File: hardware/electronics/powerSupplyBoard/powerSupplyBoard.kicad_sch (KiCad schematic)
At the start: 8 parts, among them J1 Barrel_Jack_Switch, J2 VAL, J3 VAL, J4 VAL

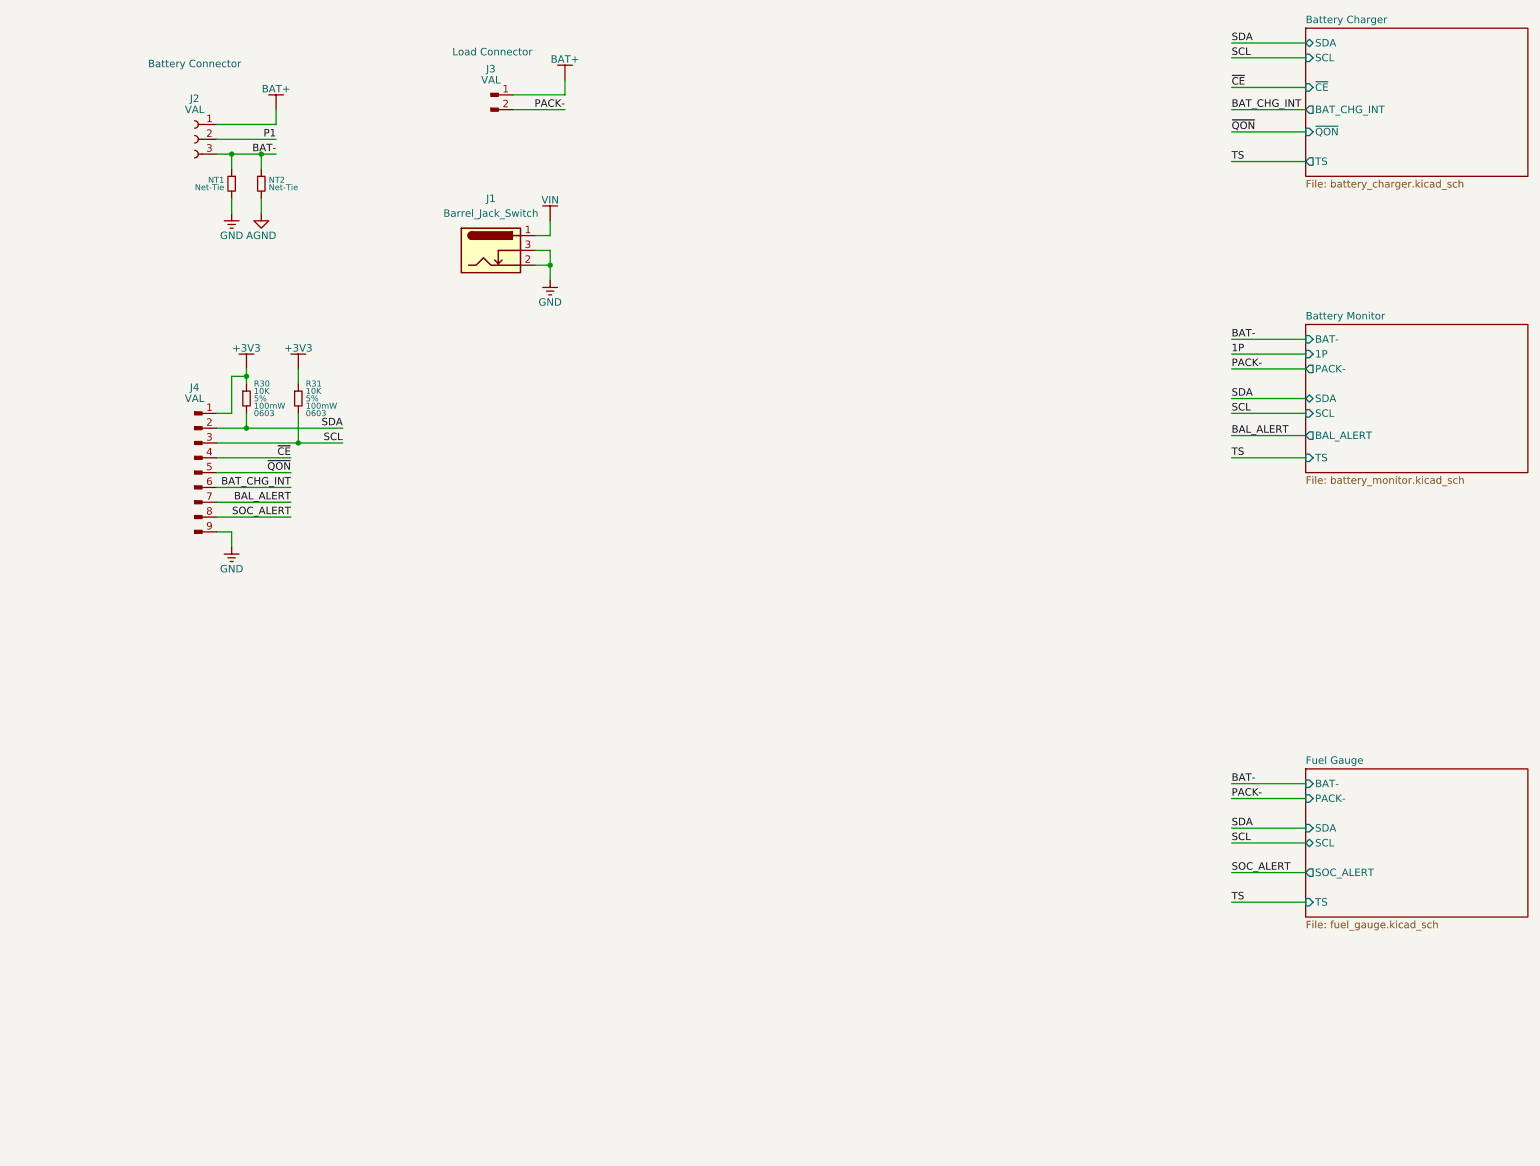
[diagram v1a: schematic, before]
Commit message: added basic sch for stm32l4
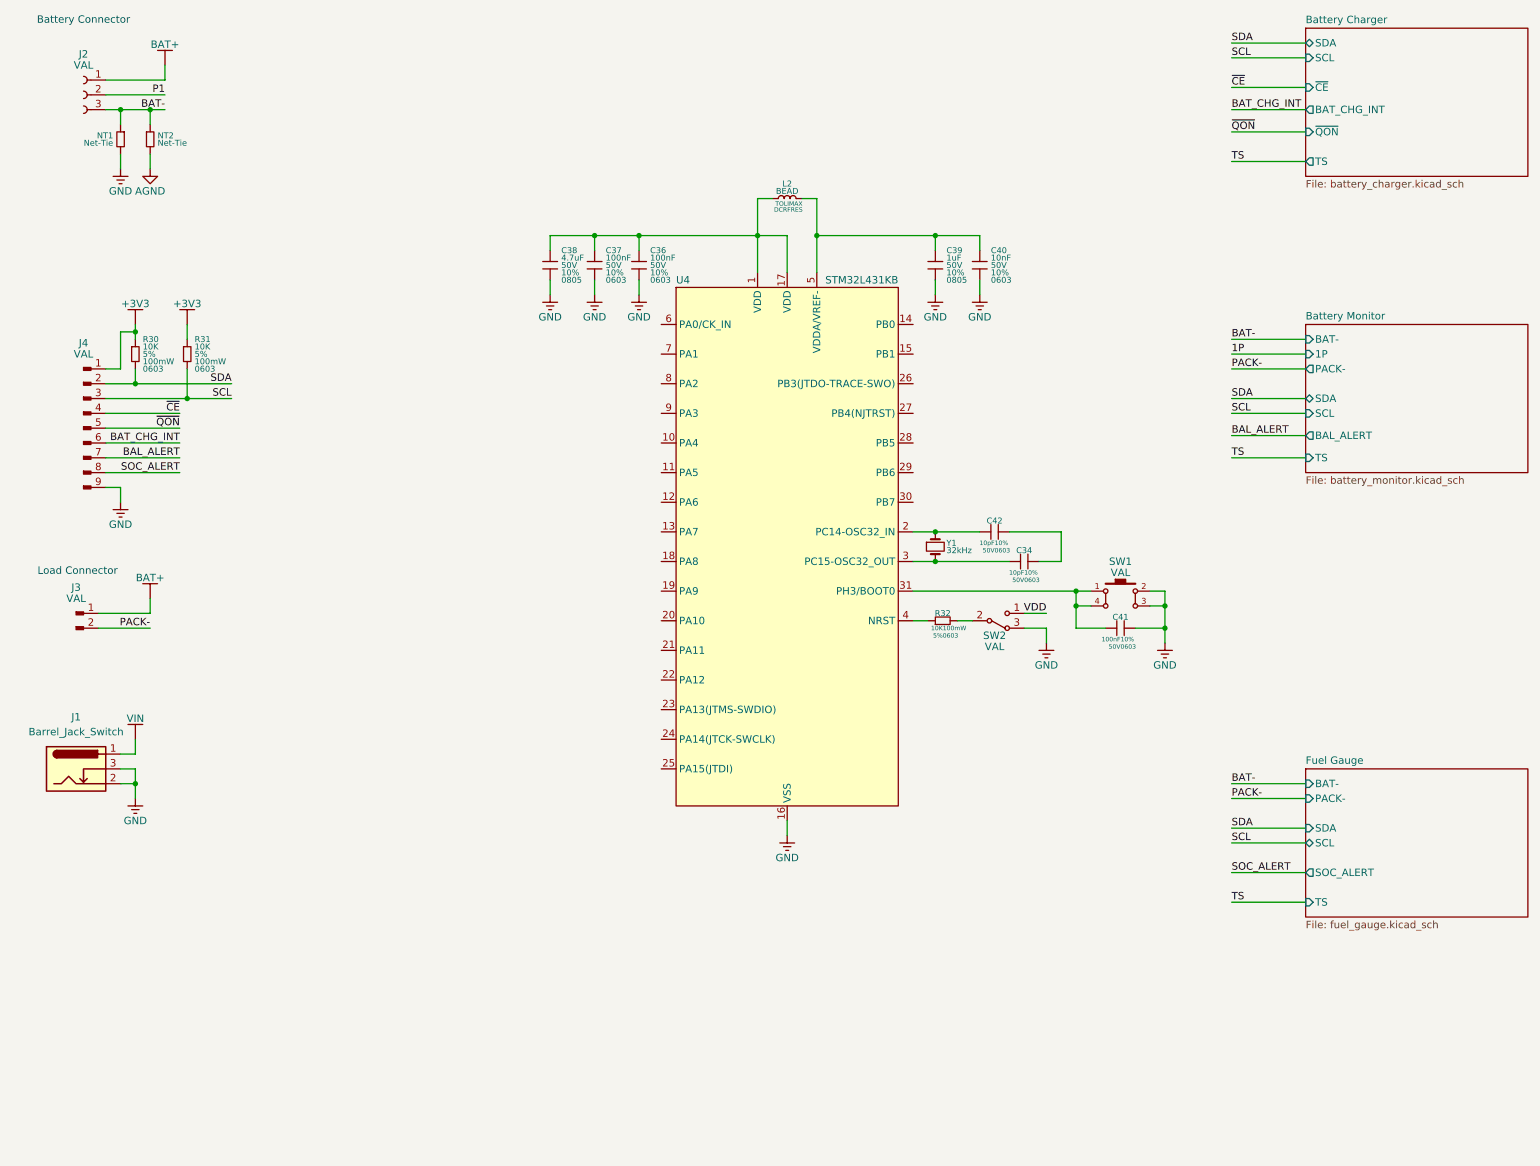
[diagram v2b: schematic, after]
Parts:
- added C34, C42: 10pF, DS-Capacitors-SMD:MLCC0603, symbol DS-Passives:C_horizontal
- added C36, C37: 100nF, DS-Capacitors-SMD:MLCC0603, symbol DS-Passives:C
- added C38: 4.7uF, DS-Capacitors-SMD:MLCC0603, symbol DS-Passives:C
- added C39: 1uF, DS-Capacitors-SMD:MLCC0805, symbol DS-Passives:C
- added C40: 10nF, DS-Capacitors-SMD:MLCC0603, symbol DS-Passives:C
- added C41: 100nF, DS-Capacitors-SMD:MLCC0603, symbol DS-Passives:C_horizontal
- added L2: BEAD, symbol DS-Passives:L_horizontal
- added R32: 10K, DS-Resistors-SMD:CRCW0603, symbol DS-Passives:R_horizontal
- added SW1: VAL, symbol DS-Switches:SPST-NO Button
- added SW2: VAL, symbol DS-Switches:SPDT
- added U4: STM32L431KB, DS-Microcontrollers:UFQFPN32, symbol DS-Micocontrollers:STM32L431KB
- added Y1: ~, symbol DS-Crystals-Oscillators-Resonators:crystal_small
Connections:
- net GND: now also C36.2, C37.2, C38.2, C39.2, C40.2, C41.2, SW1.2, SW1.3, SW2.3, U4.16 (VSS), U4.32 (VSS), U4.33 (VSS)
- new net: C36.1, C37.1, C38.1, L2.1, U4.1 (VDD), U4.17 (VDD)
- new net: C41.1, SW1.1, SW1.4, U4.31 (PH3/BOOT0)
- new net: C39.1, C40.1, L2.2, U4.5 (VDDA/VREF-)
- new net: C42.1, U4.2 (PC14-OSC32_IN), Y1.1
- new net: C34.1, U4.3 (PC15-OSC32_OUT), Y1.2
- new net: R32.2, SW2.2
- new net: R32.1, U4.4 (NRST)
- new net: C34.2, C42.2
- new net VDD: SW2.1
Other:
- moved on the sheet: J1, J2, J3, J4, NT1, NT2, R30, R31

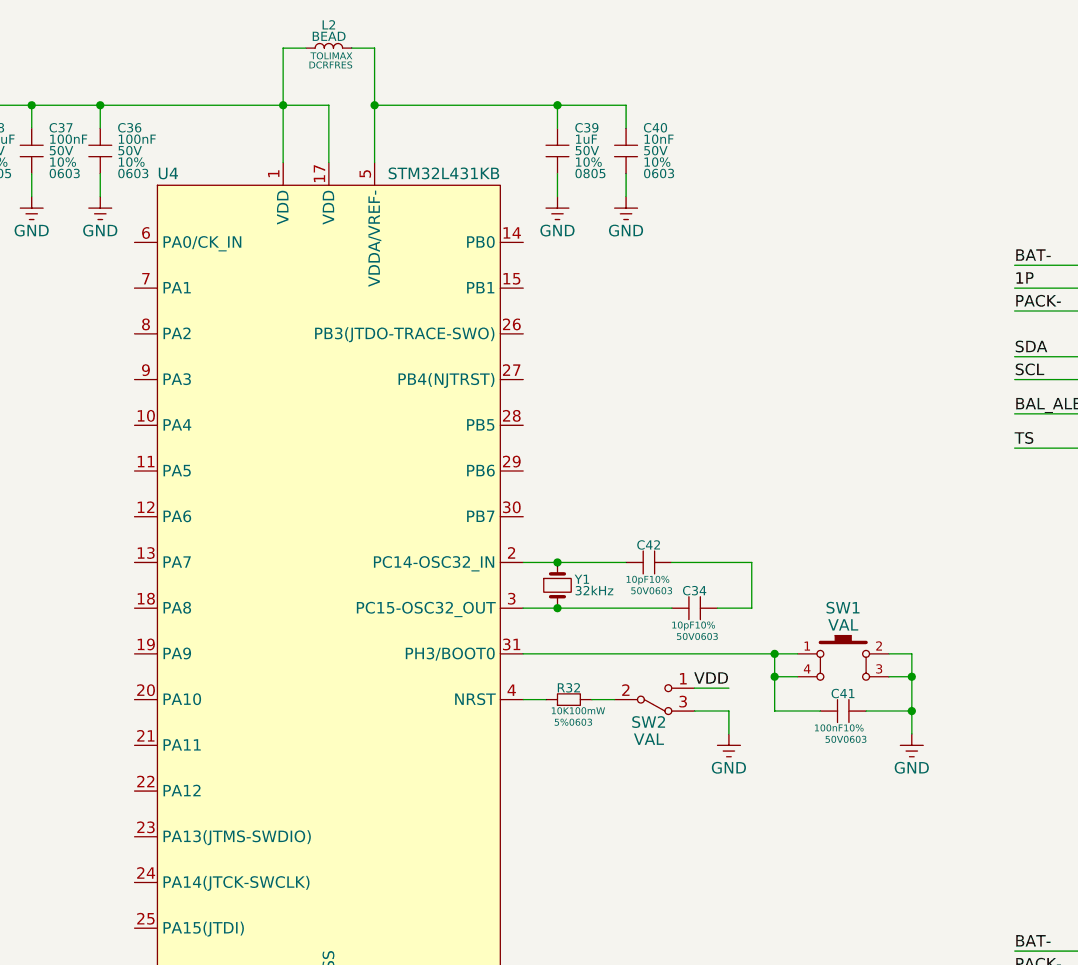
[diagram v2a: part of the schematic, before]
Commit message: replaced symbol in sch. updated crystal freq to 32.768kHz
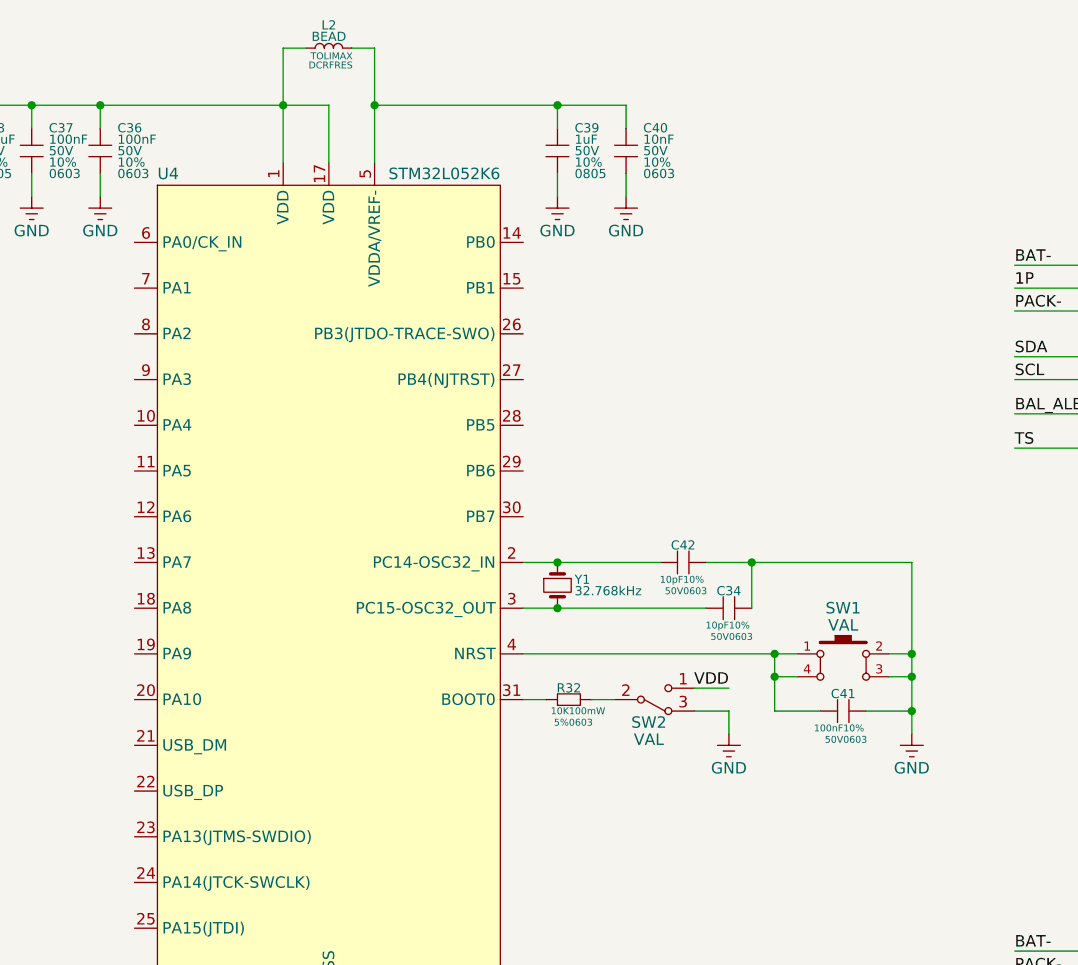
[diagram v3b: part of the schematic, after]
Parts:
- removed U4: STM32L431KB, DS-Microcontrollers:UFQFPN32, symbol DS-Micocontrollers:STM32L431KB
- added U4: STM32L052K6, symbol DS-Micocontrollers:STM32L052K6
- Y1: Frequency 32kHz -> 32.768kHz
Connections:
- net GND: now also C34.2, C42.2, U4.16 (VSS), U4.32 (VSS), U4.33 (VSS)
- net at C36.1, C37.1, C38.1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: now also U4.1 (VDD), U4.17 (VDD)
- net at C41.1, SW1.1, SW1.4: now also U4.4 (NRST)
- net at C39.1, C40.1, L2.2: now also U4.5 (VDDA/VREF-)
- net at C42.1, Y1.1: now also U4.2 (PC14-OSC32_IN)
- net at C34.1, Y1.2: now also U4.3 (PC15-OSC32_OUT)
- net at R32.1: now also U4.31 (BOOT0)
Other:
- moved on the sheet: C34, C42

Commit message: worked on first page schematic
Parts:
- removed L2: BEAD, symbol DS-Passives:L_horizontal
- removed R30, R31: 10K, DS-Resistors-SMD:CRCW0603, symbol DS-Passives:R
- added C1, C2: 10uF, DS-Capacitors-SMD:MLCC0805, symbol DS-Passives:C
- added C11: 100nF, DS-Capacitors-SMD:MLCC0603, symbol DS-Passives:C
- added J8: ~, DS-Connectors-SMD:TC2050-FP, symbol DS-Connectors:JTAG-10
- added J9: USB_C_Receptacle_USB2.0, DS-Connector-USB:MOLEX_2171790001, symbol DS-Connectors:USB_C_Receptacle_USB2.0
- added R1, R2: 5K1, DS-Resistors-SMD:CRCW0603, symbol DS-Passives:R
- added R3, R4: 10K, DS-Resistors-SMD:CRCW0603, symbol DS-Passives:R
- added R6: 120R, DS-Resistors-SMD:CRCW0603, symbol DS-Passives:R
- added U5: SN65HVD230QDR, DS-Package-SO:SOIC8P127_490X600X195L83X42N, symbol DS-ICs:SN65HVD23xQ
- added U6: AP2112K-3.3, DS-Package-SO:SOT23-5P95_280X300X110L40X38N, symbol DS-PMIC:AP2112K
- C3: renamed from C38; DKPN (none) -> 478-KGM21AR71A475MUCT-ND; MPN (none) -> 0805ZC475MAT2A; Tolerance 10% -> 20%; Voltage Rating 50V -> 10V
- C34: value 10pF -> 6pF; DKPN (none) -> 478-06035A6R0B4T2ACT-ND; MPN (none) -> 06035A6R0B4T2A; Tolerace 10% -> 1%
- C7: renamed from C40; DKPN (none) -> 478-KGM15AR71C103KTCT-ND; MPN (none) -> KGM15AR71C103KT; Voltage Rating 50V -> 16V
- C8: renamed from C42; value 10pF -> 6pF; DKPN (none) -> 478-06035A6R0B4T2ACT-ND; MPN (none) -> 06035A6R0B4T2A; Tolerace 10% -> 1%
- SW1: value VAL -> PTS647; footprint (none) -> DS-Switches:SW_4.5x4.5; DKPN (none) -> PTS647SM38SMTR2LFSCT-ND; MPN (none) -> PTS 647 SM38 SMTR2 LFS; Manufacturer (none) -> C&K
- SW2: value VAL -> SS-12D07; DKPN (none) -> CKN10397-ND; MPN (none) -> SS-12D07-VG 4 NS GA PA; Manufacturer (none) -> C&K
- U4: footprint (none) -> DS-Microcontrollers:UFQFPN32
- Y1: value ~ -> ECS-327ATQMV; footprint (none) -> DS-Crystals:EXC-34Q; DKPN (none) -> 50-ECS-.327-6-34QS-TRCT-ND; MPN (none) -> ECS-.327-6-34QS-TR; Manufacturer (none) -> ECS Inc.
- renumbered C41 to C10, C37 to C4, C36 to C5, C39 to C6, R32 to R5
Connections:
- net +3V3: now also C3.1, C4.1, C5.1, C6.1, C7.1, U4.1 (VDD), U4.17 (VDD), U4.5 (VDDA/VREF-), C11.1, C2.1, J8.1 (VCC), R3.1, R4.1, U5.3 (VCC), U6.5 (VOUT)
- net BAL_ALERT: now also U4.27 (PB4)
- net BAT_CHG_INT: now also U4.15 (PB1)
- net GND: now also C1.2, C11.2, C2.2, J8.3 (GND), J8.5 (GND), J8.9 (GNDDet), J9.A1 (GND), J9.A12 (GND), J9.B1 (GND), J9.B12 (GND), J9.S1 (SHIELD), U5.2 (GND), U6.2 (GND)
- net SCL: now also U4.29 (PB6), R4.2
- net SDA: now also U4.30 (PB7), R3.2
- net SOC_ALERT: now also U4.28 (PB5)
- net ~{CE}: now also U4.14 (PB0)
- net ~{QON}: now also U4.26 (PB3)
- net NRST: now reaches C10.1, SW1.1, SW1.4, U4.4 (NRST)
- net NRST: now also J8.10 (nRESET)
- net CAN_MODE: now reaches U4.18 (PA8)
- net CAN_MODE: now also U5.8 (RS)
- net CAN_TXD: now reaches U4.19 (PA9)
- net CAN_TXD: now also U5.1 (RXD)
- net CAN_RXD: now reaches U4.20 (PA10)
- net CAN_RXD: now also U5.4 (TXD)
- net D_N: now reaches U4.21 (PA11)
- net D_N: now also J9.A7 (D-), J9.B7 (D-)
- net D_P: now reaches U4.22 (PA12)
- net D_P: now also J9.A6 (D+), J9.B6 (D+)
- net SWDIO: now reaches U4.23 (PA13(JTMS-SWDIO))
- net SWDCLK: now reaches U4.24 (PA14(JTCK-SWCLK))
- net SWDCLK: now also J8.4 (SWDCLK)
- new net: C1.1, J9.A4 (VBUS), J9.A9 (VBUS), J9.B4 (VBUS), J9.B9 (VBUS), R1.1, R2.1, U6.1 (VIN), U6.3 (EN)
- new net: J9.A5 (CC1), R1.2
- new net: J9.B5 (CC2), R2.2
- new net: R6.2, U5.6 (CANL)
- new net: R6.1, U5.7 (CANH)
- new net SDWDIO: J8.2 (SWDIO)
- no-connect marks 0 -> 13
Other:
- note added: "Charger Connector"
- note added: "GPIO Connector"
- note added: "Tag-Connect Socket"
- note added: "USB and Voltage Regulator"
- moved on the sheet: C6, C7, J1, J2, J3, J4, NT1, NT2
